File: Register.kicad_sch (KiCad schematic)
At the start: 8 parts, among them U201 74HCT173, U202 74HCT173, U203 74HC245, U204 74HC245

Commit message: Working
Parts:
- renumbered C201 to C501, C202 to C502, C203 to C503, C204 to C504, U201 to U501, U202 to U502, U203 to U503, U204 to U504
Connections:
- net ~{OE_B}: no longer U501.10 (E2), U502.10 (E2)
- new net ~{Load}: U501.10 (E2), U502.10 (E2)

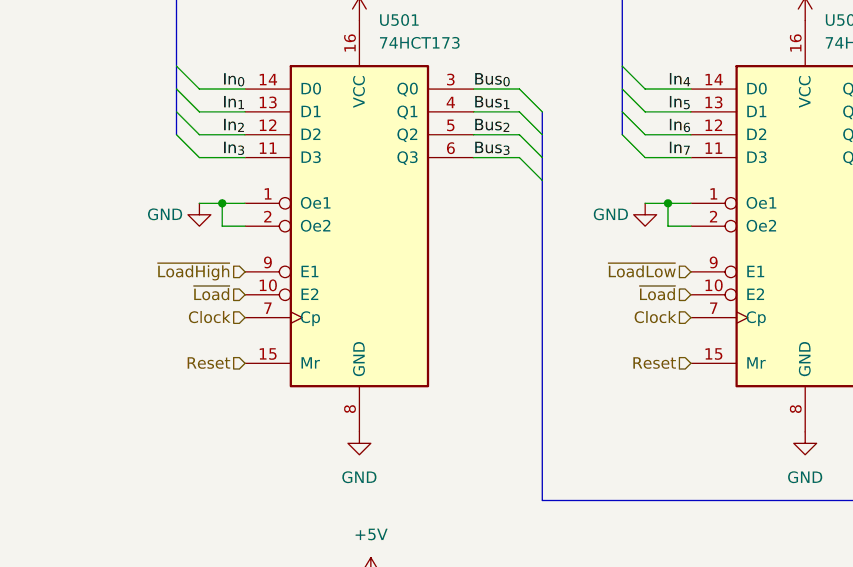
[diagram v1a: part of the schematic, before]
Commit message: Reorganize Registerfile
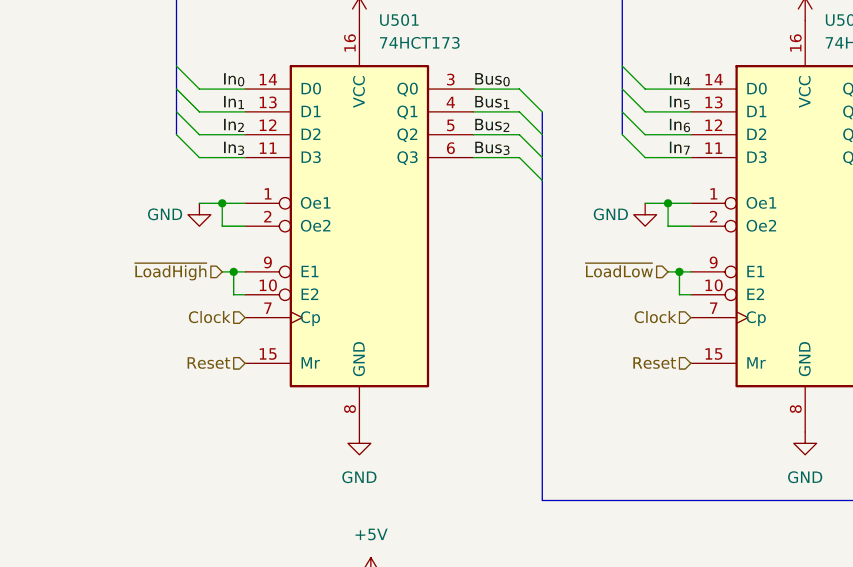
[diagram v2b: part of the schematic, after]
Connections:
- net ~{LoadHigh}: now also U501.10 (E2)
- net ~{LoadLow}: now also U502.10 (E2)
- removed net ~{Load}: U501.10 (E2), U502.10 (E2)
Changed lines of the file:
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@@
+	)
+	(junction
+		(at 92.71 63.5)
+		(diameter 0)
+		(color 0 0 0 0)
 	)
 	(junction
@@
 	)
 	(junction
+		(at 43.18 63.5)
+		(diameter 0)
+		(color 0 0 0 0)
+	)
+	(junction
 		(at 83.82 113.03)
 		(diameter 0)
@@
 		)
 	)
+	(wire
+		(pts
+			(xy 92.71 66.04) (xy 92.71 63.5)
+		)
+		(stroke
+			(width 0)
+			(type default)
+		)
+	)
 	(bus
 		(pts
@@
 		)
 	)
+	(wire
+		(pts
+			(xy 93.98 66.04) (xy 92.71 66.04)
+		)
+		(stroke
+			(width 0)
+			(type default)
+		)
+	)
 	(bus
 		(pts
@@
 		)
 	)
+	(wire
+		(pts
+			(xy 43.18 63.5) (xy 44.45 63.5)
+		)
+		(stroke
+			(width 0)
+			(type default)
+		)
+	)
 	(bus
 		(pts
@@
 		)
 	)
+	(wire
+		(pts
+			(xy 92.71 63.5) (xy 93.98 63.5)
+		)
+		(stroke
+			(width 0)
+			(type default)
+		)
+	)
 	(bus
 		(pts
@@
 	(wire
 		(pts
+			(xy 41.91 63.5) (xy 43.18 63.5)
+		)
+		(stroke
+			(width 0)
+			(type default)
+		)
+	)
+	(wire
+		(pts
 			(xy 232.41 45.72) (xy 237.49 45.72)
 		)
@@
 		)
 	)
+	(wire
+		(pts
+			(xy 91.44 63.5) (xy 92.71 63.5)
+		)
+		(stroke
+			(width 0)
+			(type default)
+		)
+	)
 	(bus
 		(pts
@@
 		)
 	)
+	(wire
+		(pts
+			(xy 43.18 66.04) (xy 44.45 66.04)
+		)
+		(stroke
+			(width 0)
+			(type default)
+		)
+	)
 	(bus
 		(pts
@@
 		(pts
 			(xy 232.41 48.26) (xy 237.49 48.26)
+		)
+		(stroke
+			(width 0)
+			(type default)
+		)
+	)
+	(wire
+		(pts
+			(xy 43.18 63.5) (xy 43.18 66.04)
 		)
 		(stroke
@@
 	(hierarchical_label "~{LoadHigh}"
 		(shape input)
-		(at 44.45 63.5 180)
+		(at 41.91 63.5 180)
 		(effects
 			(font
@@
 	(hierarchical_label "~{LoadLow}"
 		(shape input)
-		(at 93.98 63.5 180)
+		(at 91.44 63.5 180)
 		(effects
 			(font
@@
 		)
 	)
-	(hierarchical_label "~{Load}"
-		(shape input)
-		(at 44.45 66.04 180)
-		(effects
-			(font
-				(size 1.27 1.27)
-			)
-			(justify right)
-		)
-	)
 	(hierarchical_label "B_{[0..7]}"
 		(shape output)
@@
 		)
 	)
-	(hierarchical_label "~{Load}"
-		(shape input)
-		(at 93.98 66.04 180)
-		(effects
-			(font
-				(size 1.27 1.27)
-			)
-			(justify right)
-		)
-	)

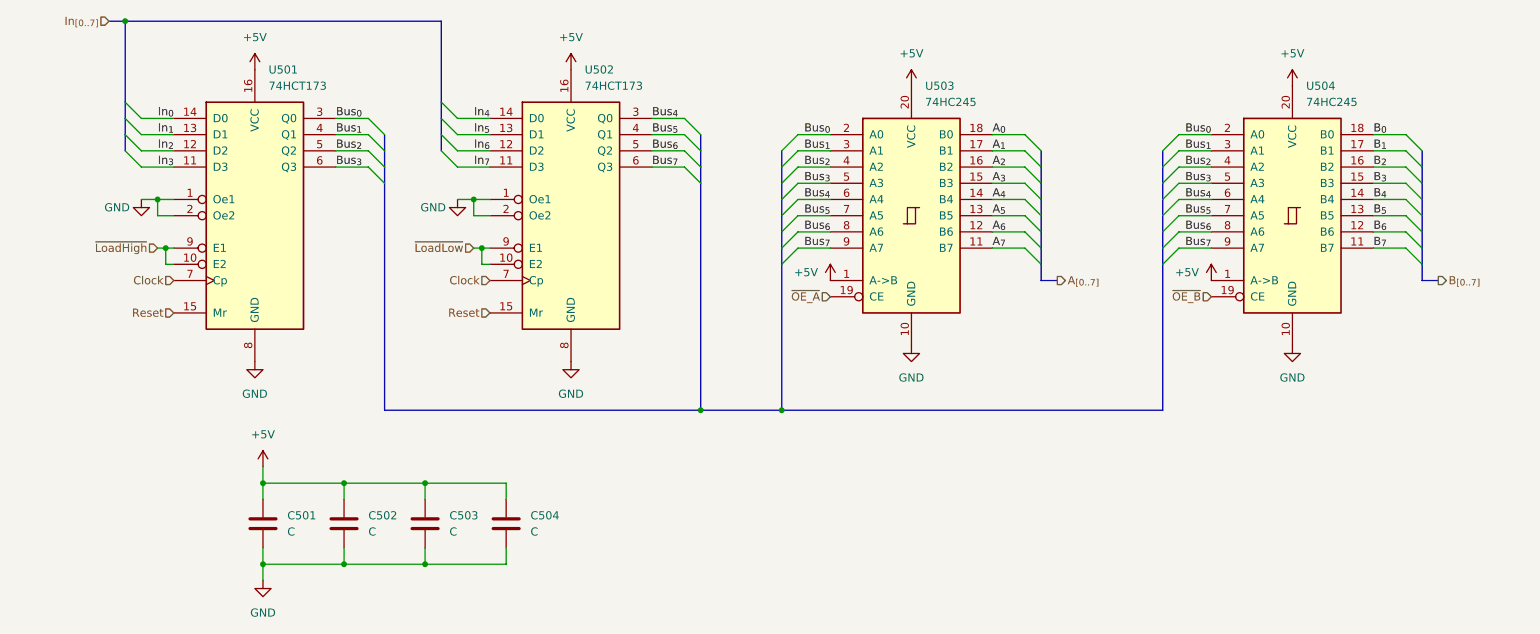
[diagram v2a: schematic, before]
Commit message: More cleanup and preparing signals for control logic
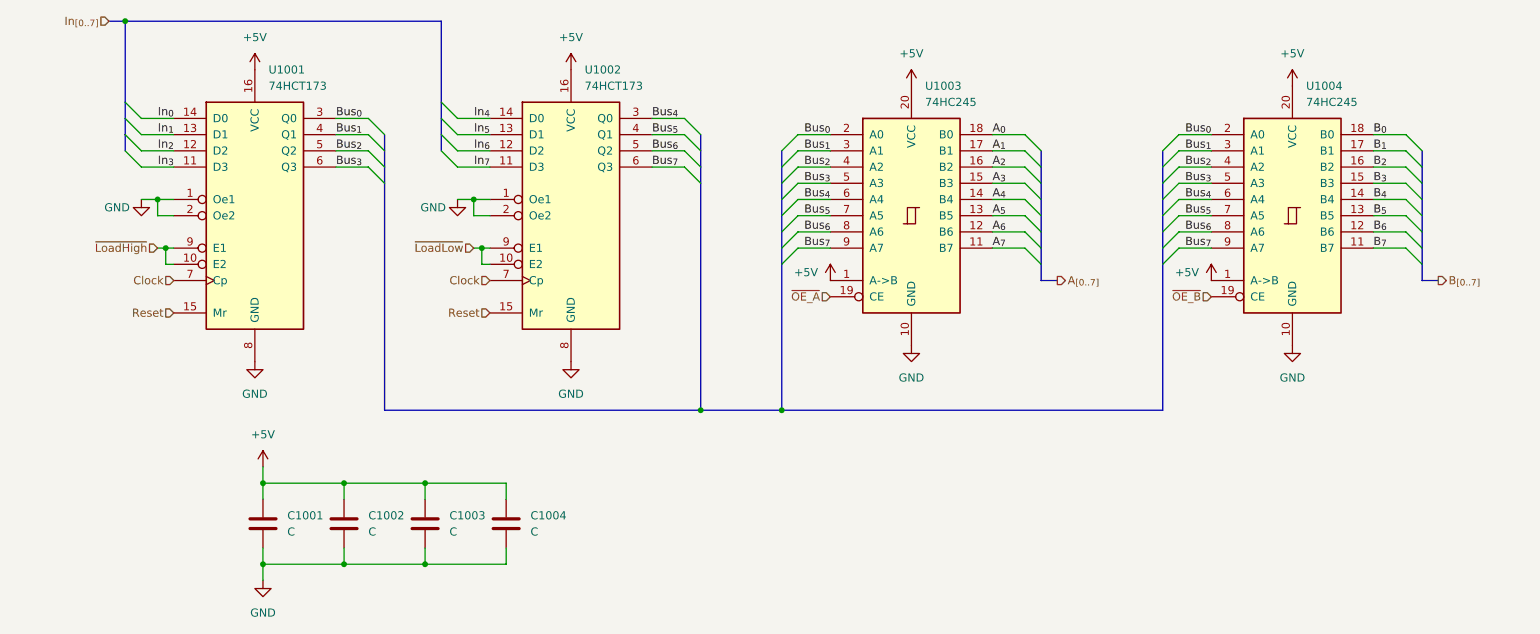
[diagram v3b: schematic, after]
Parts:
- renumbered C501 to C1001, C502 to C1002, C503 to C1003, C504 to C1004, U501 to U1001, U502 to U1002, U503 to U1003, U504 to U1004

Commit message: Draft Schematic
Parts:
- C1001, C1002, C1003, C1004: value C -> 0.1uF; footprint (none) -> Capacitor_THT:C_Rect_L4.0mm_W2.5mm_P2.50mm
- U1001, U1002: value 74HCT173 -> 74HC173; footprint (none) -> Package_DIP:DIP-16_W7.62mm
- U1003, U1004: footprint (none) -> Package_DIP:DIP-20_W7.62mm
